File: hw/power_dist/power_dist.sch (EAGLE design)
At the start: 67 parts, among them J1 JST-ZH6SMT_VERT, J2 JST-PH4SMT_VERT, J3 JST-PH5VERT, P1 XT30P, P2 XT30P, P3 XT30P, P4 XT30P, P5 XT30P, P6 XT30P, P7 XT90PW-M, Q1 PSMN4R8-100BSEJ, Q2 PSMN4R8-100BSEJ, Q3 PSMN4R8-100BSEJ, Q4 MF-DSC-SOT233-BSS138, Q5 MF-DSC-SOT233-MMBT3906, Q6 MF-DSC-SOT233-MMBT3904, U1 MAX15062AATA+T, U2 STM32G474CEU6, U3 LM5066IPMHE/NOPB, U4 TCAN334G

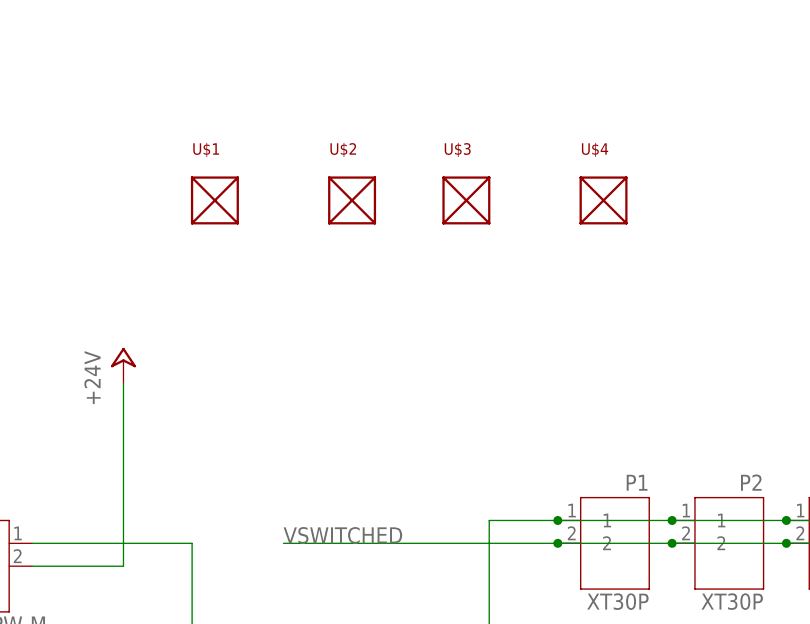
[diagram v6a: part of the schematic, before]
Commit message: power_dist r4: Optionally ground one of the mounting holes
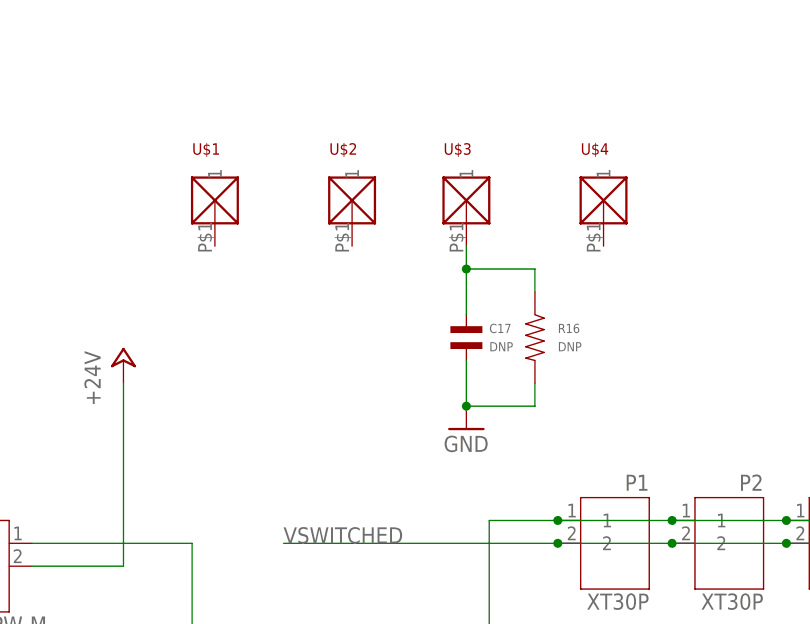
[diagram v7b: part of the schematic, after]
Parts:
- added C17: DNP, mfpassives:CAPACITOR_NP_0603
- added R16: DNP, mfpassives:RESISTOR_0603
- U$1, U$2, U$3, U$4: device precharge:MOUNT -> power_dist:MOUNT
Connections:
- new net N$15: C17.P$1, R16.P$1, U$3.1
- net GND: now also C17.P$2, R16.P$2
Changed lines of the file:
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@@
 <parts>
 <part name="GND8" library="supply1" deviceset="GND" device=""/>
-<part name="U$1" library="precharge" deviceset="MOUNT" device="" value="MOUNT">
+<part name="U$1" library="power_dist" deviceset="MOUNT" device="" value="MOUNT">
 <attribute name="POPULATE" value="0"/>
 </part>
-<part name="U$2" library="precharge" deviceset="MOUNT" device="" value="MOUNT">
+<part name="U$2" library="power_dist" deviceset="MOUNT" device="" value="MOUNT">
 <attribute name="POPULATE" value="0"/>
 </part>
-<part name="U$3" library="precharge" deviceset="MOUNT" device="" value="MOUNT">
+<part name="U$3" library="power_dist" deviceset="MOUNT" device="" value="MOUNT">
 <attribute name="POPULATE" value="0"/>
 </part>
-<part name="U$4" library="precharge" deviceset="MOUNT" device="" value="MOUNT">
+<part name="U$4" library="power_dist" deviceset="MOUNT" device="" value="MOUNT">
 <attribute name="POPULATE" value="0"/>
 </part>
@@
 <part name="Q6" library="mfdiscretesemi" deviceset="NPN_BJT" device="_SOT-23-3" technology="MMBT3904" value="MF-DSC-SOT233-MMBT3904"/>
 <part name="GND25" library="supply1" deviceset="GND" device=""/>
+<part name="C17" library="mfpassives" deviceset="CAPACITOR_NP" device="_0603" value="DNP">
+<attribute name="HOUSEPART" value="1"/>
+<attribute name="MPN" value="MF-CAP-0603-1uF"/>
+</part>
+<part name="GND26" library="supply1" deviceset="GND" device=""/>
+<part name="R16" library="mfpassives" deviceset="RESISTOR" device="_0603" value="DNP"/>
 </parts>
 <sheets>
@@
 <attribute name="VALUE" x="63.5" y="-91.44" size="1.778" layer="96"/>
 </instance>
+<instance part="C17" gate="G$1" x="0" y="162.56" smashed="yes">
+<attribute name="NAME" x="2.54" y="164.084" size="1.016" layer="95" font="vector" align="top-left"/>
+<attribute name="VALUE" x="2.54" y="161.036" size="1.016" layer="96" font="vector"/>
+</instance>
+<instance part="GND26" gate="1" x="0" y="152.4" smashed="yes">
+<attribute name="VALUE" x="-2.54" y="149.86" size="1.778" layer="96"/>
+</instance>
+<instance part="R16" gate="G$1" x="7.62" y="162.56" smashed="yes">
+<attribute name="NAME" x="10.16" y="164.084" size="1.016" layer="95" font="vector" align="top-left"/>
+<attribute name="VALUE" x="10.16" y="161.036" size="1.016" layer="96" font="vector"/>
+</instance>
 </instances>
 <busses>
@@
 <pinref part="GND25" gate="1" pin="GND"/>
 <wire x1="66.04" y1="-83.82" x2="66.04" y2="-86.36" width="0.1524" layer="91"/>
+</segment>
+<segment>
+<pinref part="GND26" gate="1" pin="GND"/>
+<pinref part="C17" gate="G$1" pin="P$2"/>
+<wire x1="0" y1="154.94" x2="0" y2="160.02" width="0.1524" layer="91"/>
+<pinref part="R16" gate="G$1" pin="P$2"/>
+<wire x1="7.62" y1="157.48" x2="7.62" y2="154.94" width="0.1524" layer="91"/>
+<wire x1="7.62" y1="154.94" x2="0" y2="154.94" width="0.1524" layer="91"/>
+<junction x="0" y="154.94"/>
 </segment>
 </net>
@@
 </segment>
 </net>
+<net name="N$15" class="0">
+<segment>
+<pinref part="U$3" gate="G$1" pin="1"/>
+<wire x1="0" y1="172.72" x2="0" y2="170.18" width="0.1524" layer="91"/>
+<pinref part="C17" gate="G$1" pin="P$1"/>
+<pinref part="R16" gate="G$1" pin="P$1"/>
+<wire x1="0" y1="170.18" x2="0" y2="165.1" width="0.1524" layer="91"/>
+<wire x1="7.62" y1="167.64" x2="7.62" y2="170.18" width="0.1524" layer="91"/>
+<wire x1="7.62" y1="170.18" x2="0" y2="170.18" width="0.1524" layer="91"/>
+<junction x="0" y="170.18"/>
+</segment>
+</net>

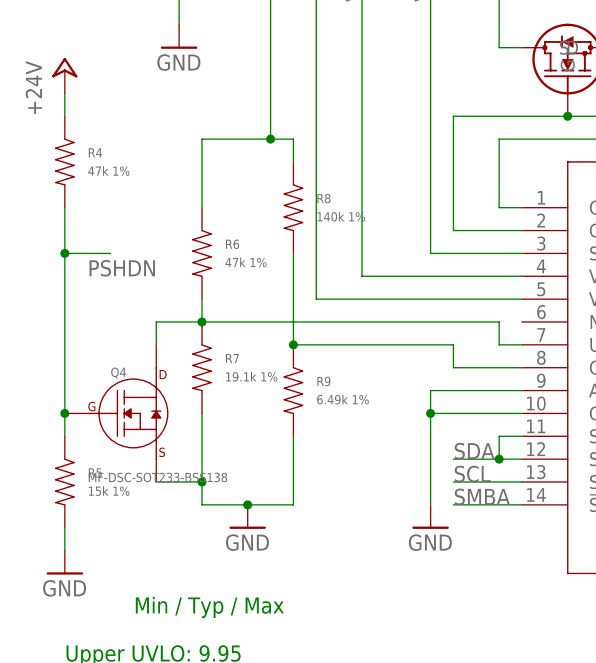
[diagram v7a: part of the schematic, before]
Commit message: power_dist r4: Assign part numbers
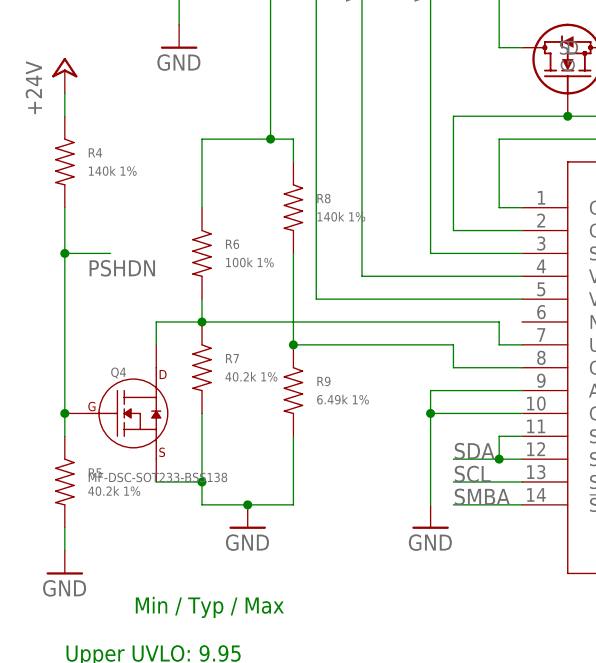
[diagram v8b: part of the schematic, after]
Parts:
- C17: HOUSEPART 1 -> (none); MPN MF-CAP-0603-1uF -> (none); POPULATE (none) -> 0
- D2, Q4, Q5, Q6: HOUSEPART (none) -> 1
- J3: MF (none) -> JST; MPN (none) -> B5B-PH-SM4-TB(LF)(SN); POPULATE (none) -> 1
- P1, P2, P3, P4, P5, P6: MF (none) -> AMASS; MPN (none) -> XT30UPB-F; POPULATE 0 -> 1
- R11: MF (none) -> YAGEO; MPN (none) -> RC0603FR-0724KL
- R12: MF (none) -> YAGEO; MPN (none) -> RC0603FR-071KL
- R16: POPULATE (none) -> 0
- R4: value 47k 1% -> 140k 1%; MF (none) -> YAGEO; MPN (none) -> RC0603FR-07140KL
- R5: value 15k 1% -> 40.2k 1%; MF (none) -> YAGEO; MPN (none) -> RC0603FR-0740K2L
- R6: value 47k 1% -> 100k 1%; MF (none) -> YAGEO; MPN (none) -> RC0603FR-07100KL
- R7: value 19.1k 1% -> 40.2k 1%; MF (none) -> YAGEO; MPN (none) -> RC0603FR-0740K2L
- R8: MF (none) -> YAGEO; MPN (none) -> RC0603FR-07140KL
- R9: MF (none) -> YAGEO; MPN (none) -> RC0603FR-076K49L
- U3: MF (none) -> TI; MPN (none) -> LM5066IPMHE/NOPB; POPULATE (none) -> 1
